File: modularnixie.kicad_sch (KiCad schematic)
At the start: 36 parts, among them J1 Feed, J2 Feed, Q1 MMBT5551, Q10 MMBT5551, Q11 MMBT5551, Q12 MMBT5551, Q13 MMBT5551, Q14 MMBT5551, Q15 MMBT5551, Q16 MMBT5551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

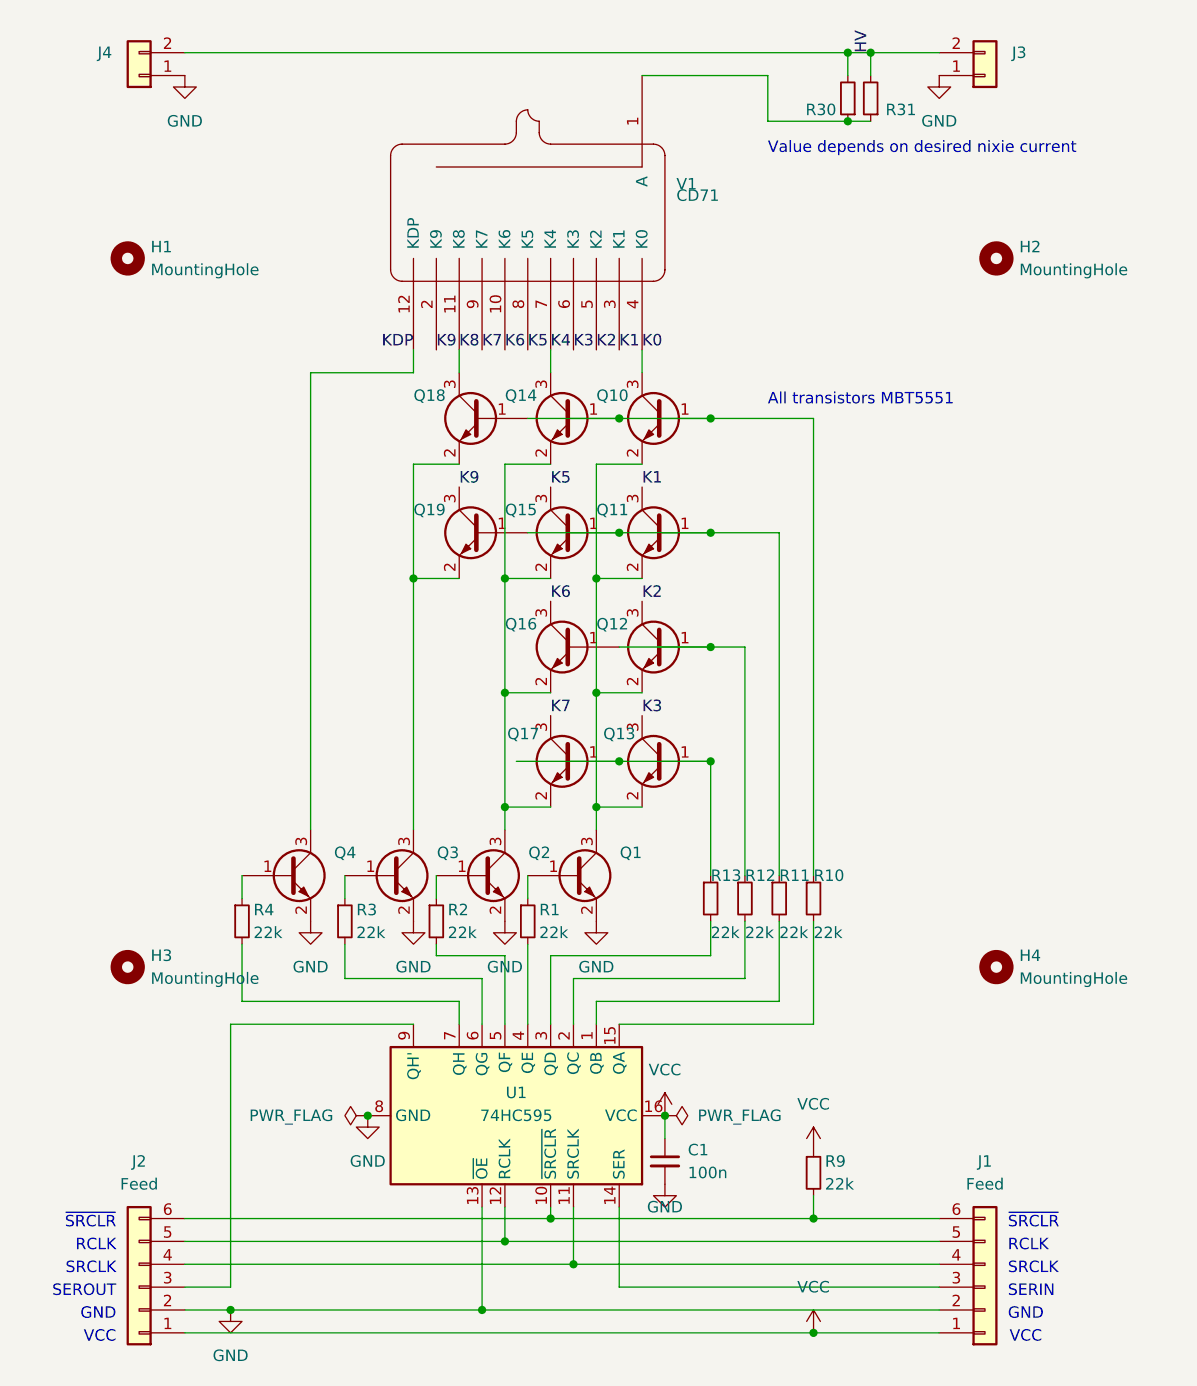
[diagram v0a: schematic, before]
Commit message: Stray wire, transistor type typo
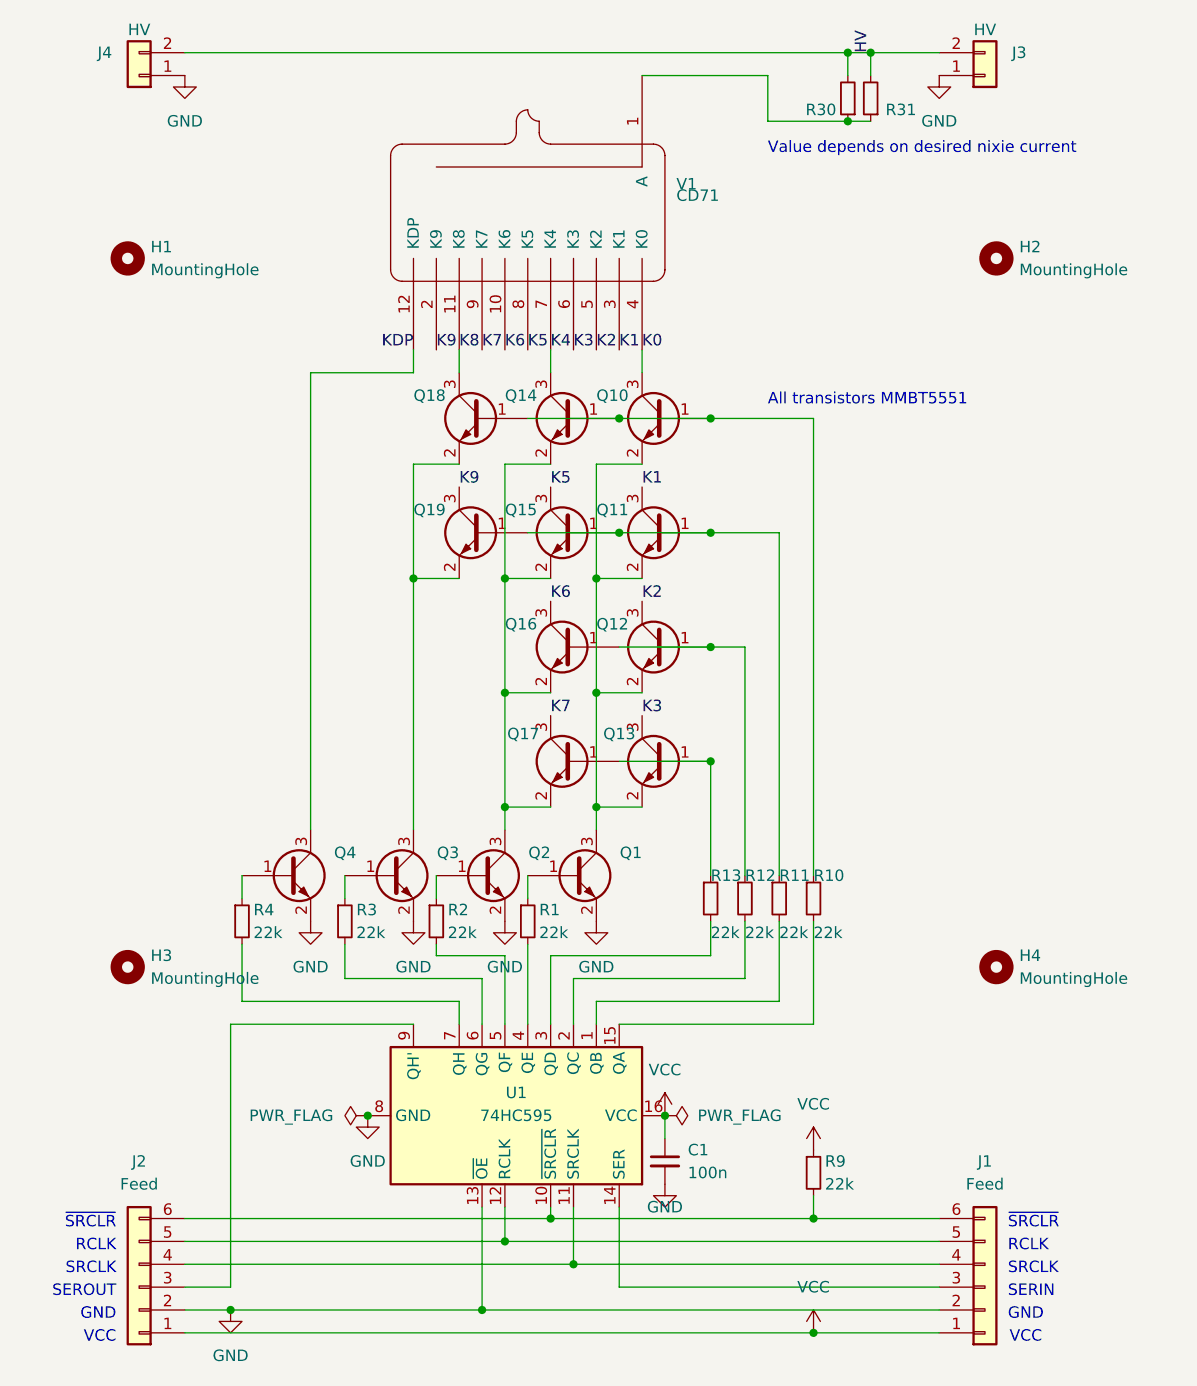
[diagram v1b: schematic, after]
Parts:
- J3, J4: value (none) -> HV
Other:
- note added: "All transistors MMBT5551"
- note removed: "All transistors MBT5551"
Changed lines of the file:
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@@
   (junction (at 77.47 90.17) (diameter 0) (color 0 0 0 0)
   )
-  (junction (at 80.01 97.79) (diameter 0) (color 0 0 0 0)
-  )
   (junction (at 67.31 102.87) (diameter 0) (color 0 0 0 0)
   )
@@
   )
   (wire (pts (xy 85.09 137.16) (xy 85.09 139.7))
-    (stroke (width 0) (type default) (color 0 0 0 0))
-  )
-  (wire (pts (xy 68.58 97.79) (xy 80.01 97.79))
     (stroke (width 0) (type default) (color 0 0 0 0))
   )
@@
     (effects (font (size 1.27 1.27)) (justify left bottom))
   )
-  (text "All transistors MBT5551" (at 96.52 58.42 0)
+  (text "All transistors MMBT5551" (at 96.52 58.42 0)
     (effects (font (size 1.27 1.27)) (justify left bottom))
   )
@@
     (in_bom yes) (on_board yes)
     (property "Reference" "J4" (id 0) (at 22.86 19.05 0))
-    (property "Value" "" (id 1) (at 26.67 16.51 0))
+    (property "Value" "HV" (id 1) (at 26.67 16.51 0))
     (property "Footprint" "Connector_PinHeader_2.54mm:PinHeader_1x02_P2.54mm_Vertical" (id 2) (at 26.67 21.59 0)
       (effects (font (size 1.27 1.27)) hide)
@@
     (in_bom yes) (on_board yes)
     (property "Reference" "J3" (id 0) (at 124.46 19.05 0))
-    (property "Value" "" (id 1) (at 120.65 16.51 0))
+    (property "Value" "HV" (id 1) (at 120.65 16.51 0))
     (property "Footprint" "Connector_PinHeader_2.54mm:PinHeader_1x02_P2.54mm_Vertical" (id 2) (at 120.65 21.59 0)
       (effects (font (size 1.27 1.27)) hide)

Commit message: Actually replace SOP-16 with SOIC-16 to get 3D model
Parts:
- U1: footprint Package_SO:SOP-16_3.9x9.9mm_P1.27mm -> Package_SO:SOIC-16_3.9x9.9mm_P1.27mm
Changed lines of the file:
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@@
     (property "Reference" "U1" (id 0) (at 68.58 134.62 90))
     (property "Value" "74HC595" (id 1) (at 68.58 137.16 90))
-    (property "Footprint" "Package_SO:SOP-16_3.9x9.9mm_P1.27mm" (id 2) (at 69.85 137.16 0)
+    (property "Footprint" "Package_SO:SOIC-16_3.9x9.9mm_P1.27mm" (id 2) (at 69.85 137.16 0)
       (effects (font (size 1.27 1.27)) hide)
     )
@@
     )
     (path "/7bc13ee4-2194-461b-9242-0d96ebba241b"
-      (reference "U1") (unit 1) (value "74HC595") (footprint "Package_SO:SOP-16_3.9x9.9mm_P1.27mm")
+      (reference "U1") (unit 1) (value "74HC595") (footprint "Package_SO:SOIC-16_3.9x9.9mm_P1.27mm")
     )
     (path "/fc12372f-6e31-40f9-8043-b00b861f0171"
